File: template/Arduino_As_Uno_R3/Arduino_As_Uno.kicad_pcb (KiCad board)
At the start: 2 copper layers, 68.6 x 53.3 mm, 4 parts, among them P1 Power, P2 Analog, P3 Digital, P4 Digital

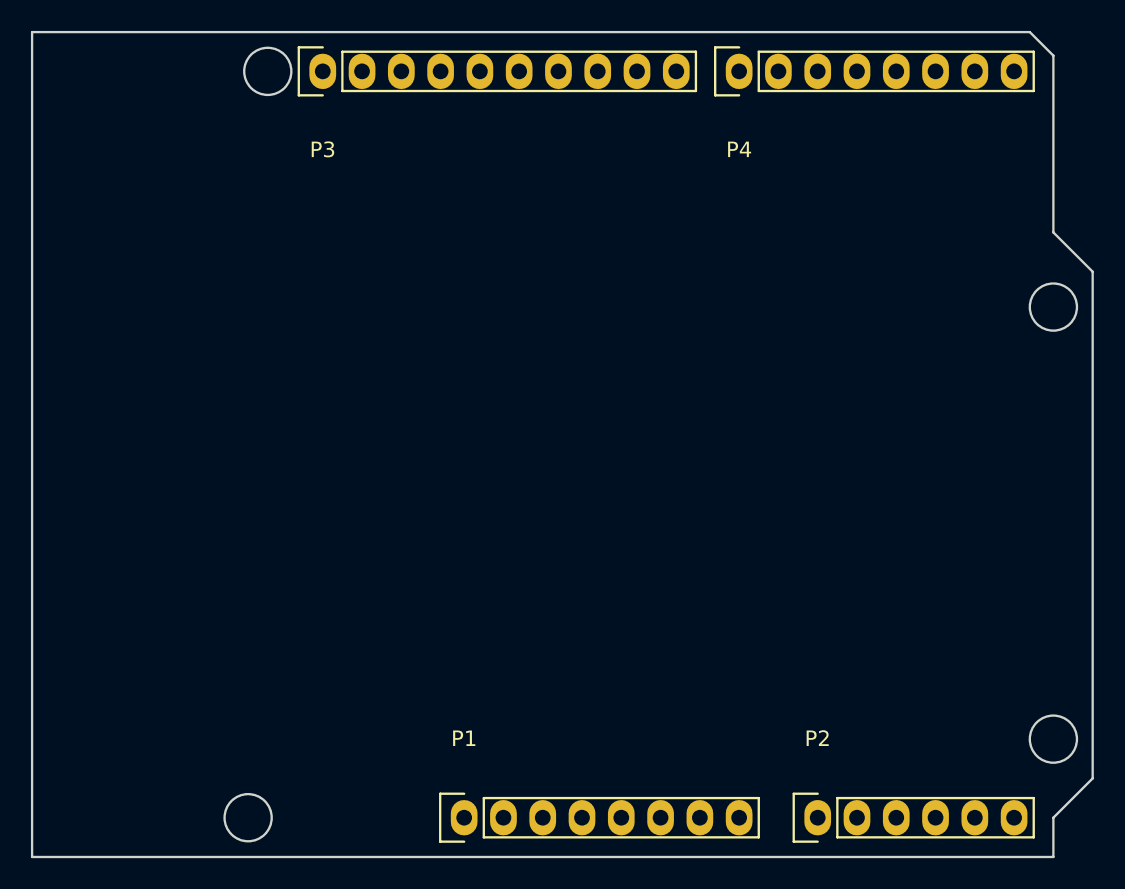
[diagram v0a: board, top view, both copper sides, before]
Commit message: corrections pads and holes
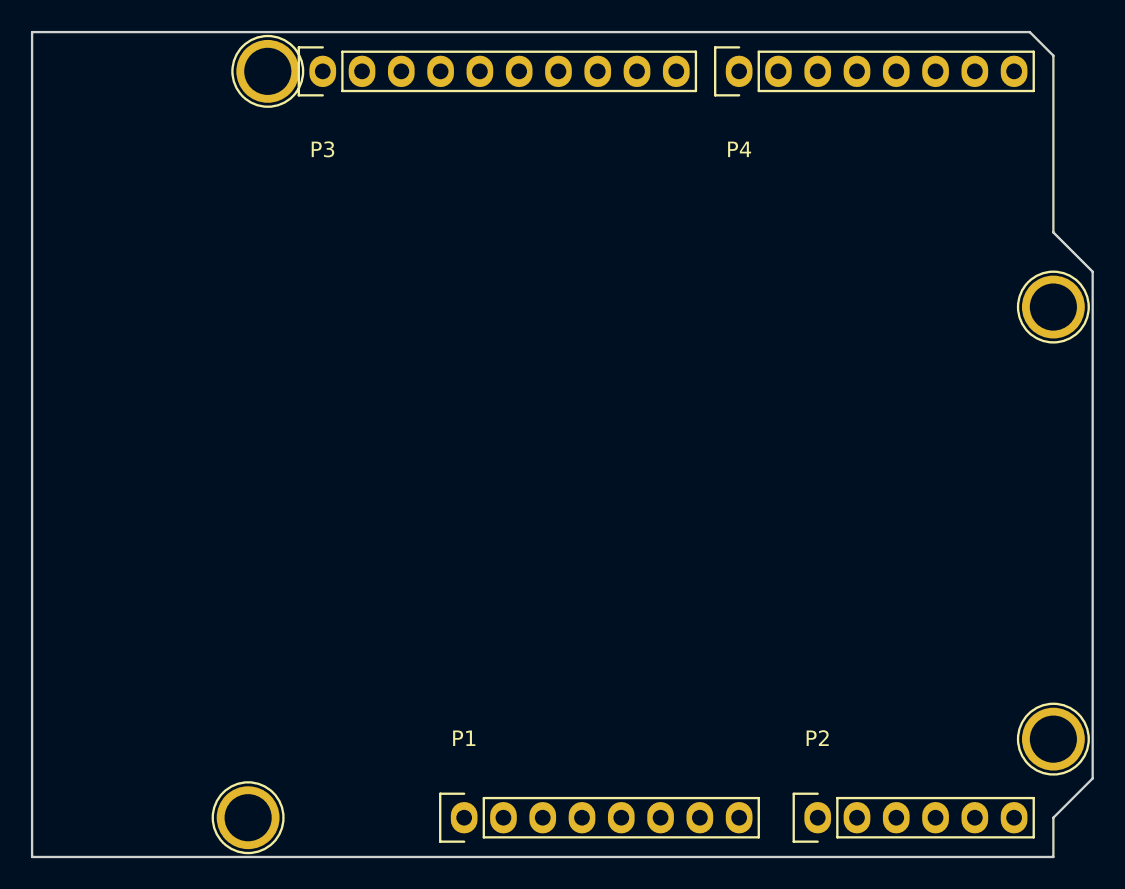
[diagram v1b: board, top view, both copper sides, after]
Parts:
- added REF**: 1pin, Connect:1pin, F.Cu at (126.2, 75.6)
- added REF**: 1pin, Connect:1pin, F.Cu at (177.0, 90.8)
- added REF**: 1pin, Connect:1pin, F.Cu at (125.0, 123.8)
- added REF**: 1pin, Connect:1pin, F.Cu at (177.0, 118.7)
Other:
- outline, holes or cut-outs redrawn

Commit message: correction holes
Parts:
- removed REF** (x4): 1pin, Connect:1pin
- added P5: CONN_1, Connect:1pin, F.Cu at (125.0, 123.8)
- added P6: CONN_1, Connect:1pin, F.Cu at (177.0, 118.7)
- added P7: CONN_1, Connect:1pin, F.Cu at (126.2, 75.6)
- added P8: CONN_1, Connect:1pin, F.Cu at (177.0, 90.8)
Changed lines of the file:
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@@
     (zones 0)
     (modules 8)
-    (nets 29)
+    (nets 33)
   )
   (page A4)
@@
   (net 27 "/1(Tx)")
   (net 28 "/0(Rx)")
+  (net 29 "Net-(P5-Pad1)")
+  (net 30 "Net-(P6-Pad1)")
+  (net 31 "Net-(P7-Pad1)")
+  (net 32 "Net-(P8-Pad1)")
   (net_class Default "This is the default net class."
     (clearance 0.2)
@@
     (add_net /Vin)
     (add_net GND)
-  )
-  (module Connect:1pin (layer F.Cu)
-    (at 126.238 75.565)
-    (descr "module 1 pin (ou trou mecanique de percage)")
-    (tags DEV)
-    (fp_text reference REF** (at 0 -3.048) (layer F.SilkS) hide
-      (effects (font (size 1 1) (thickness 0.15)))
-    )
-    (fp_text value 1pin (at 0 2.794) (layer F.Fab) hide
-      (effects (font (size 1 1) (thickness 0.15)))
-    )
-    (fp_circle (center 0 0) (end 0 -2.286) (layer F.SilkS) (width 0.15))
-    (pad "" thru_hole circle (at 0 0) (size 4.064 4.064) (drill 3.048) (layers *.Cu *.Mask))
-  )
-  (module Connect:1pin (layer F.Cu)
-    (at 177.038 90.805)
-    (descr "module 1 pin (ou trou mecanique de percage)")
-    (tags DEV)
-    (fp_text reference REF** (at 0 -3.048) (layer F.SilkS) hide
-      (effects (font (size 1 1) (thickness 0.15)))
-    )
-    (fp_text value 1pin (at 0 2.794) (layer F.Fab) hide
-      (effects (font (size 1 1) (thickness 0.15)))
-    )
-    (fp_circle (center 0 0) (end 0 -2.286) (layer F.SilkS) (width 0.15))
-    (pad "" thru_hole circle (at 0 0) (size 4.064 4.064) (drill 3.048) (layers *.Cu *.Mask F.SilkS))
-  )
-  (module Connect:1pin (layer F.Cu)
-    (at 124.968 123.825)
-    (descr "module 1 pin (ou trou mecanique de percage)")
-    (tags DEV)
-    (fp_text reference REF** (at 0 -3.048) (layer F.SilkS) hide
-      (effects (font (size 1 1) (thickness 0.15)))
-    )
-    (fp_text value 1pin (at 0 2.794) (layer F.Fab) hide
-      (effects (font (size 1 1) (thickness 0.15)))
-    )
-    (fp_circle (center 0 0) (end 0 -2.286) (layer F.SilkS) (width 0.15))
-    (pad "" thru_hole circle (at 0 0) (size 4.064 4.064) (drill 3.048) (layers *.Cu *.Mask F.SilkS))
-  )
-  (module Connect:1pin (layer F.Cu)
-    (at 177.038 118.745)
-    (descr "module 1 pin (ou trou mecanique de percage)")
-    (tags DEV)
-    (fp_text reference REF** (at 0 -3.048) (layer F.SilkS) hide
-      (effects (font (size 1 1) (thickness 0.15)))
-    )
-    (fp_text value 1pin (at 0 2.794) (layer F.Fab) hide
-      (effects (font (size 1 1) (thickness 0.15)))
-    )
-    (fp_circle (center 0 0) (end 0 -2.286) (layer F.SilkS) (width 0.15))
-    (pad "" thru_hole circle (at 0 0) (size 4.064 4.064) (drill 3.048) (layers *.Cu *.Mask F.SilkS))
+    (add_net "Net-(P5-Pad1)")
+    (add_net "Net-(P6-Pad1)")
+    (add_net "Net-(P7-Pad1)")
+    (add_net "Net-(P8-Pad1)")
   )
   (module Socket_Arduino_Uno:Socket_Strip_Arduino_1x08 (layer F.Cu)
@@
     )
   )
+  (module Connect:1pin (layer F.Cu)
+    (at 124.968 123.825)
+    (descr "module 1 pin (ou trou mecanique de percage)")
+    (tags DEV)
+    (fp_text reference P5 (at 0 -3.048) (layer F.SilkS) hide
+      (effects (font (size 1 1) (thickness 0.15)))
+    )
+    (fp_text value CONN_1 (at 0 2.794) (layer F.Fab) hide
+      (effects (font (size 1 1) (thickness 0.15)))
+    )
+    (fp_circle (center 0 0) (end 0 -2.286) (layer F.SilkS) (width 0.15))
+    (pad "" thru_hole circle (at 0 0) (size 4.064 4.064) (drill 3.048) (layers *.Cu *.Mask F.SilkS)
+      (net 29 "Net-(P5-Pad1)"))
+  )
+  (module Connect:1pin (layer F.Cu)
+    (at 177.038 118.745)
+    (descr "module 1 pin (ou trou mecanique de percage)")
+    (tags DEV)
+    (fp_text reference P6 (at 0 -3.048) (layer F.SilkS) hide
+      (effects (font (size 1 1) (thickness 0.15)))
+    )
+    (fp_text value CONN_1 (at 0 2.794) (layer F.Fab) hide
+      (effects (font (size 1 1) (thickness 0.15)))
+    )
+    (fp_circle (center 0 0) (end 0 -2.286) (layer F.SilkS) (width 0.15))
+    (pad "" thru_hole circle (at 0 0) (size 4.064 4.064) (drill 3.048) (layers *.Cu *.Mask F.SilkS)
+      (net 30 "Net-(P6-Pad1)"))
+  )
+  (module Connect:1pin (layer F.Cu)
+    (at 126.238 75.565)
+    (descr "module 1 pin (ou trou mecanique de percage)")
+    (tags DEV)
+    (fp_text reference P7 (at 0 -3.048) (layer F.SilkS) hide
+      (effects (font (size 1 1) (thickness 0.15)))
+    )
+    (fp_text value CONN_1 (at 0 2.794) (layer F.Fab) hide
+      (effects (font (size 1 1) (thickness 0.15)))
+    )
+    (fp_circle (center 0 0) (end 0 -2.286) (layer F.SilkS) (width 0.15))
+    (pad "" thru_hole circle (at 0 0) (size 4.064 4.064) (drill 3.048) (layers *.Cu *.Mask F.SilkS)
+      (net 31 "Net-(P7-Pad1)"))
+  )
+  (module Connect:1pin (layer F.Cu)
+    (at 177.038 90.805)
+    (descr "module 1 pin (ou trou mecanique de percage)")
+    (tags DEV)
+    (fp_text reference P8 (at 0 -3.048) (layer F.SilkS) hide
+      (effects (font (size 1 1) (thickness 0.15)))
+    )
+    (fp_text value CONN_1 (at 0 2.794) (layer F.Fab) hide
+      (effects (font (size 1 1) (thickness 0.15)))
+    )
+    (fp_circle (center 0 0) (end 0 -2.286) (layer F.SilkS) (width 0.15))
+    (pad "" thru_hole circle (at 0 0) (size 4.064 4.064) (drill 3.048) (layers *.Cu *.Mask F.SilkS)
+      (net 32 "Net-(P8-Pad1)"))
+  )
   (gr_circle (center 117.348 76.962) (end 118.618 76.962) (layer Dwgs.User) (width 0.15))

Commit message: correct num holes and add Nano board
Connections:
- net /10(**) renamed /10(**/SS)
- net /11(**) renamed /11(**/MISO)
- net /12 renamed /12(MOSI)
- net /13 renamed /13(SCK)
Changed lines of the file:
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@@
   (net 13 "/A4(SDA)")
   (net 14 "/A5(SCL)")
-  (net 15 /13)
-  (net 16 /12)
-  (net 17 "/11(**)")
-  (net 18 "/10(**)")
-  (net 19 "/9(**)")
-  (net 20 /8)
-  (net 21 /7)
-  (net 22 "/6(**)")
-  (net 23 "/5(**)")
-  (net 24 /4)
-  (net 25 "/3(**)")
-  (net 26 /2)
-  (net 27 "/1(Tx)")
-  (net 28 "/0(Rx)")
-  (net 29 "Net-(P5-Pad1)")
-  (net 30 "Net-(P6-Pad1)")
-  (net 31 "Net-(P7-Pad1)")
-  (net 32 "Net-(P8-Pad1)")
+  (net 15 "/9(**)")
+  (net 16 /8)
+  (net 17 /7)
+  (net 18 "/6(**)")
+  (net 19 "/5(**)")
+  (net 20 /4)
+  (net 21 "/3(**)")
+  (net 22 /2)
+  (net 23 "/1(Tx)")
+  (net 24 "/0(Rx)")
+  (net 25 "Net-(P5-Pad1)")
+  (net 26 "Net-(P6-Pad1)")
+  (net 27 "Net-(P7-Pad1)")
+  (net 28 "Net-(P8-Pad1)")
+  (net 29 "/13(SCK)")
+  (net 30 "/12(MOSI)")
+  (net 31 "/11(**/MISO)")
+  (net 32 "/10(**/SS)")
   (net_class Default "This is the default net class."
     (clearance 0.2)
@@
     (add_net "/0(Rx)")
     (add_net "/1(Tx)")
-    (add_net "/10(**)")
-    (add_net "/11(**)")
-    (add_net /12)
-    (add_net /13)
+    (add_net "/10(**/SS)")
+    (add_net "/11(**/MISO)")
+    (add_net "/12(MOSI)")
+    (add_net "/13(SCK)")
     (add_net /2)
     (add_net "/3(**)")
@@
       (net 6 GND))
     (pad 5 thru_hole oval (at 10.16 0) (size 1.7272 2.032) (drill 1.016) (layers *.Cu *.Mask F.SilkS)
-      (net 15 /13))
-    (pad 6 thru_hole oval (at 12.7 0) (size 1.7272 2.032) (drill 1.016) (layers *.Cu *.Mask F.SilkS)
-      (net 16 /12))
+      (net 29 "/13(SCK)"))
+    (pad 6 thru_hole oval (at 12.7 0) (size 1.7272 2.032) (drill 1.016) (layers *.Cu *.Mask F.SilkS)
+      (net 30 "/12(MOSI)"))
     (pad 7 thru_hole oval (at 15.24 0) (size 1.7272 2.032) (drill 1.016) (layers *.Cu *.Mask F.SilkS)
-      (net 17 "/11(**)"))
+      (net 31 "/11(**/MISO)"))
     (pad 8 thru_hole oval (at 17.78 0) (size 1.7272 2.032) (drill 1.016) (layers *.Cu *.Mask F.SilkS)
-      (net 18 "/10(**)"))
+      (net 32 "/10(**/SS)"))
     (pad 9 thru_hole oval (at 20.32 0) (size 1.7272 2.032) (drill 1.016) (layers *.Cu *.Mask F.SilkS)
-      (net 19 "/9(**)"))
+      (net 15 "/9(**)"))
     (pad 10 thru_hole oval (at 22.86 0) (size 1.7272 2.032) (drill 1.016) (layers *.Cu *.Mask F.SilkS)
-      (net 20 /8))
+      (net 16 /8))
     (model ${KIPRJMOD}/Socket_Arduino_Uno.3dshapes/Socket_header_Arduino_1x10.wrl
       (at (xyz 0.45 0 0))
@@
     (fp_line (start -1.55 -1.55) (end -1.55 1.55) (layer F.SilkS) (width 0.15))
     (pad 1 thru_hole oval (at 0 0) (size 1.7272 2.032) (drill 1.016) (layers *.Cu *.Mask F.SilkS)
-      (net 21 /7))
-    (pad 2 thru_hole oval (at 2.54 0) (size 1.7272 2.032) (drill 1.016) (layers *.Cu *.Mask F.SilkS)
-      (net 22 "/6(**)"))
-    (pad 3 thru_hole oval (at 5.08 0) (size 1.7272 2.032) (drill 1.016) (layers *.Cu *.Mask F.SilkS)
-      (net 23 "/5(**)"))
-    (pad 4 thru_hole oval (at 7.62 0) (size 1.7272 2.032) (drill 1.016) (layers *.Cu *.Mask F.SilkS)
-      (net 24 /4))
-    (pad 5 thru_hole oval (at 10.16 0) (size 1.7272 2.032) (drill 1.016) (layers *.Cu *.Mask F.SilkS)
-      (net 25 "/3(**)"))
-    (pad 6 thru_hole oval (at 12.7 0) (size 1.7272 2.032) (drill 1.016) (layers *.Cu *.Mask F.SilkS)
-      (net 26 /2))
+      (net 17 /7))
+    (pad 2 thru_hole oval (at 2.54 0) (size 1.7272 2.032) (drill 1.016) (layers *.Cu *.Mask F.SilkS)
+      (net 18 "/6(**)"))
+    (pad 3 thru_hole oval (at 5.08 0) (size 1.7272 2.032) (drill 1.016) (layers *.Cu *.Mask F.SilkS)
+      (net 19 "/5(**)"))
+    (pad 4 thru_hole oval (at 7.62 0) (size 1.7272 2.032) (drill 1.016) (layers *.Cu *.Mask F.SilkS)
+      (net 20 /4))
+    (pad 5 thru_hole oval (at 10.16 0) (size 1.7272 2.032) (drill 1.016) (layers *.Cu *.Mask F.SilkS)
+      (net 21 "/3(**)"))
+    (pad 6 thru_hole oval (at 12.7 0) (size 1.7272 2.032) (drill 1.016) (layers *.Cu *.Mask F.SilkS)
+      (net 22 /2))
     (pad 7 thru_hole oval (at 15.24 0) (size 1.7272 2.032) (drill 1.016) (layers *.Cu *.Mask F.SilkS)
-      (net 27 "/1(Tx)"))
+      (net 23 "/1(Tx)"))
     (pad 8 thru_hole oval (at 17.78 0) (size 1.7272 2.032) (drill 1.016) (layers *.Cu *.Mask F.SilkS)
-      (net 28 "/0(Rx)"))
+      (net 24 "/0(Rx)"))
     (model ${KIPRJMOD}/Socket_Arduino_Uno.3dshapes/Socket_header_Arduino_1x08.wrl
       (at (xyz 0.35 0 0))
@@
     )
     (fp_circle (center 0 0) (end 0 -2.286) (layer F.SilkS) (width 0.15))
-    (pad "" thru_hole circle (at 0 0) (size 4.064 4.064) (drill 3.048) (layers *.Cu *.Mask F.SilkS)
-      (net 29 "Net-(P5-Pad1)"))
+    (pad 1 thru_hole circle (at 0 0) (size 4.064 4.064) (drill 3.048) (layers *.Cu *.Mask F.SilkS)
+      (net 25 "Net-(P5-Pad1)"))
   )
   (module Connect:1pin (layer F.Cu)
@@
     )
     (fp_circle (center 0 0) (end 0 -2.286) (layer F.SilkS) (width 0.15))
-    (pad "" thru_hole circle (at 0 0) (size 4.064 4.064) (drill 3.048) (layers *.Cu *.Mask F.SilkS)
-      (net 30 "Net-(P6-Pad1)"))
+    (pad 1 thru_hole circle (at 0 0) (size 4.064 4.064) (drill 3.048) (layers *.Cu *.Mask F.SilkS)
+      (net 26 "Net-(P6-Pad1)"))
   )
   (module Connect:1pin (layer F.Cu)
@@
     )
     (fp_circle (center 0 0) (end 0 -2.286) (layer F.SilkS) (width 0.15))
-    (pad "" thru_hole circle (at 0 0) (size 4.064 4.064) (drill 3.048) (layers *.Cu *.Mask F.SilkS)
-      (net 31 "Net-(P7-Pad1)"))
+    (pad 1 thru_hole circle (at 0 0) (size 4.064 4.064) (drill 3.048) (layers *.Cu *.Mask F.SilkS)
+      (net 27 "Net-(P7-Pad1)"))
   )
   (module Connect:1pin (layer F.Cu)
@@
     )
     (fp_circle (center 0 0) (end 0 -2.286) (layer F.SilkS) (width 0.15))
-    (pad "" thru_hole circle (at 0 0) (size 4.064 4.064) (drill 3.048) (layers *.Cu *.Mask F.SilkS)
-      (net 32 "Net-(P8-Pad1)"))
+    (pad 1 thru_hole circle (at 0 0) (size 4.064 4.064) (drill 3.048) (layers *.Cu *.Mask F.SilkS)
+      (net 28 "Net-(P8-Pad1)"))
   )
   (gr_circle (center 117.348 76.962) (end 118.618 76.962) (layer Dwgs.User) (width 0.15))
